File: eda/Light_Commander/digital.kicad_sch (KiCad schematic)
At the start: 36 parts, among them J14 USB_C_Receptacle_USB2.0_16P, Q1 MMBT3904, Q2 MMBT3904, Q3 MMBT3904, Q4 MMBT3904, SW2 SW_Push, U1 STM32F446RETx, U6 USBLC6-2SC6, Y1 8 MHz

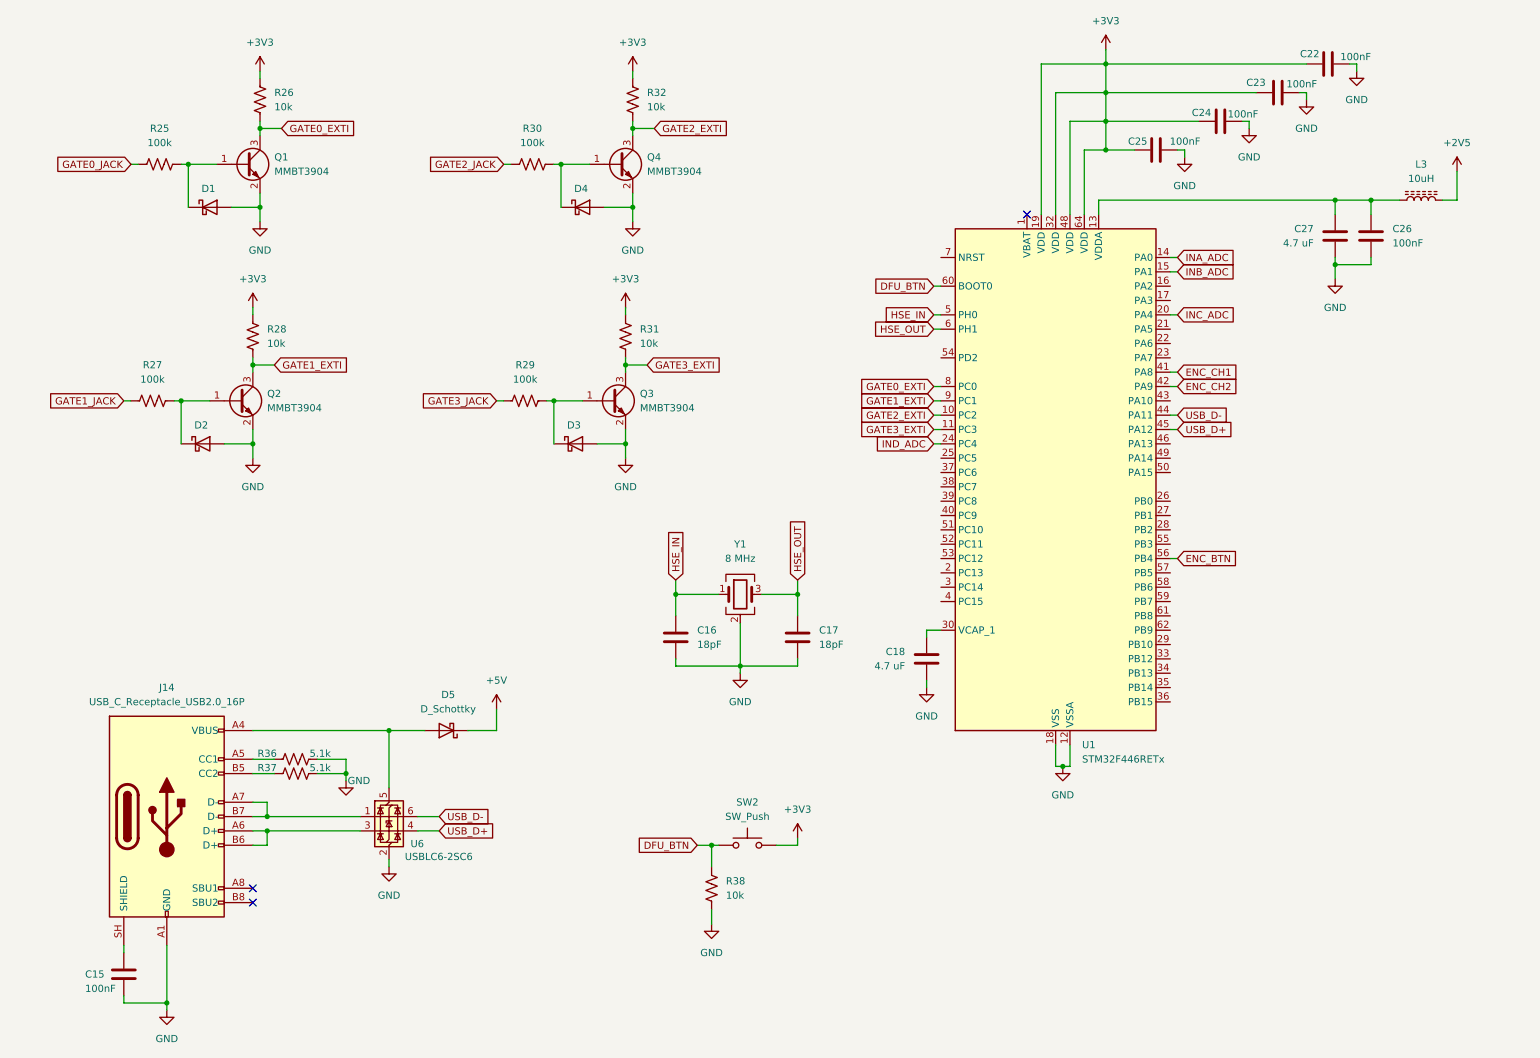
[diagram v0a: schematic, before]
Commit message: Add OLED, LED strip connector, and LED level shifter to schematic
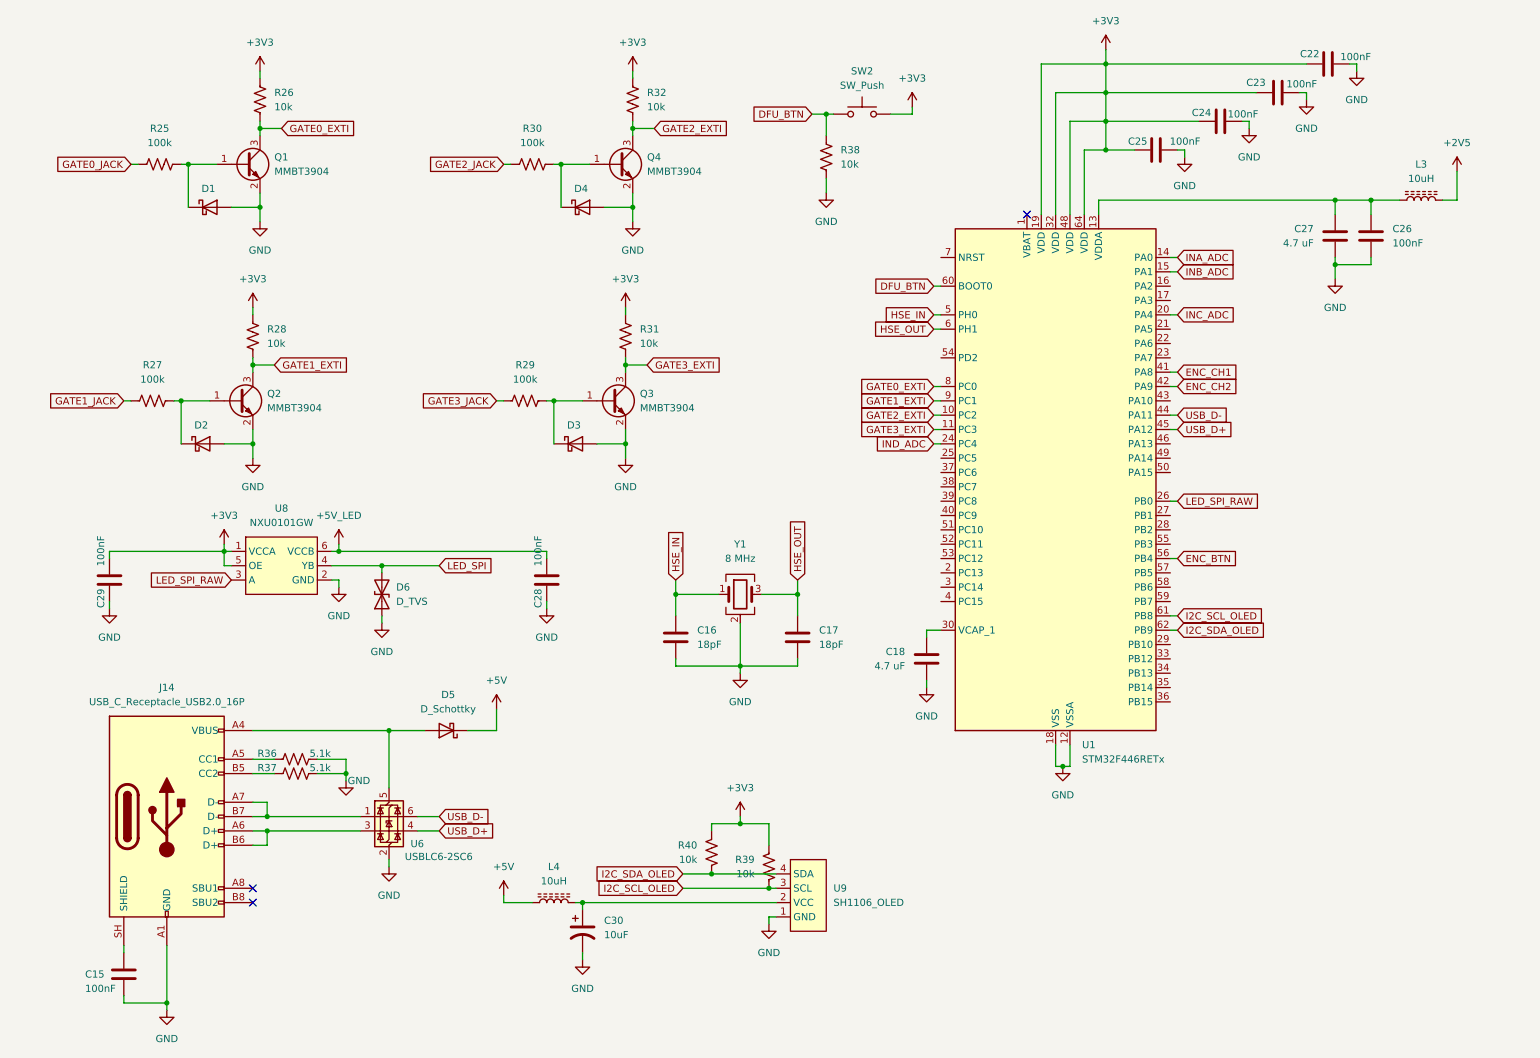
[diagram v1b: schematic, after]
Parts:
- added C28, C29: 100nF, Capacitor_SMD:C_0805_2012Metric, symbol Device:C
- added C30: 10uF, Capacitor_SMD:C_Elec_6.3x7.7, symbol Device:C_Polarized_US
- added D6: D_TVS, Diode_SMD:D_SOD-123F, symbol Device:D_TVS
- added L4: 10uH, Inductor_SMD:L_1210_3225Metric, symbol Device:L_Ferrite
- added R39, R40: 10k, Resistor_SMD:R_0805_2012Metric, symbol Device:R_US
- added U8: NXU0101GW, Package_TO_SOT_SMD:SOT-363_SC-70-6, symbol NXU0101GW:NXU0101GW
- added U9: SH1106_OLED, footprints:SH1106_1.3in_OLED, symbol SH1106_OLED:SH1106_OLED
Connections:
- net +3V3: now also C29.1, R39.1, R40.1, U8.1 (VCCA), U8.5 (OE)
- net +5V: now also L4.1
- net GND: now also C28.2, C29.2, C30.2, D6.1 (A1), U8.2 (GND), U9.1 (GND)
- net LED_SPI_RAW: now reaches U1.26 (PB0)
- net LED_SPI_RAW: now also U8.3 (A)
- net I2C_SCL_OLED: now reaches U1.61 (PB8)
- net I2C_SCL_OLED: now also R39.2, U9.3 (SCL)
- net I2C_SDA_OLED: now reaches U1.62 (PB9)
- net I2C_SDA_OLED: now also R40.2, U9.4 (SDA)
- new net: C30.1, L4.2, U9.2 (VCC)
- new net +5V_LED: C28.1, U8.6 (VCCB)
- new net LED_SPI: D6.2 (A2), U8.4 (YB)
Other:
- moved on the sheet: R38, SW2

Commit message: Add MDI in and thru to schematic
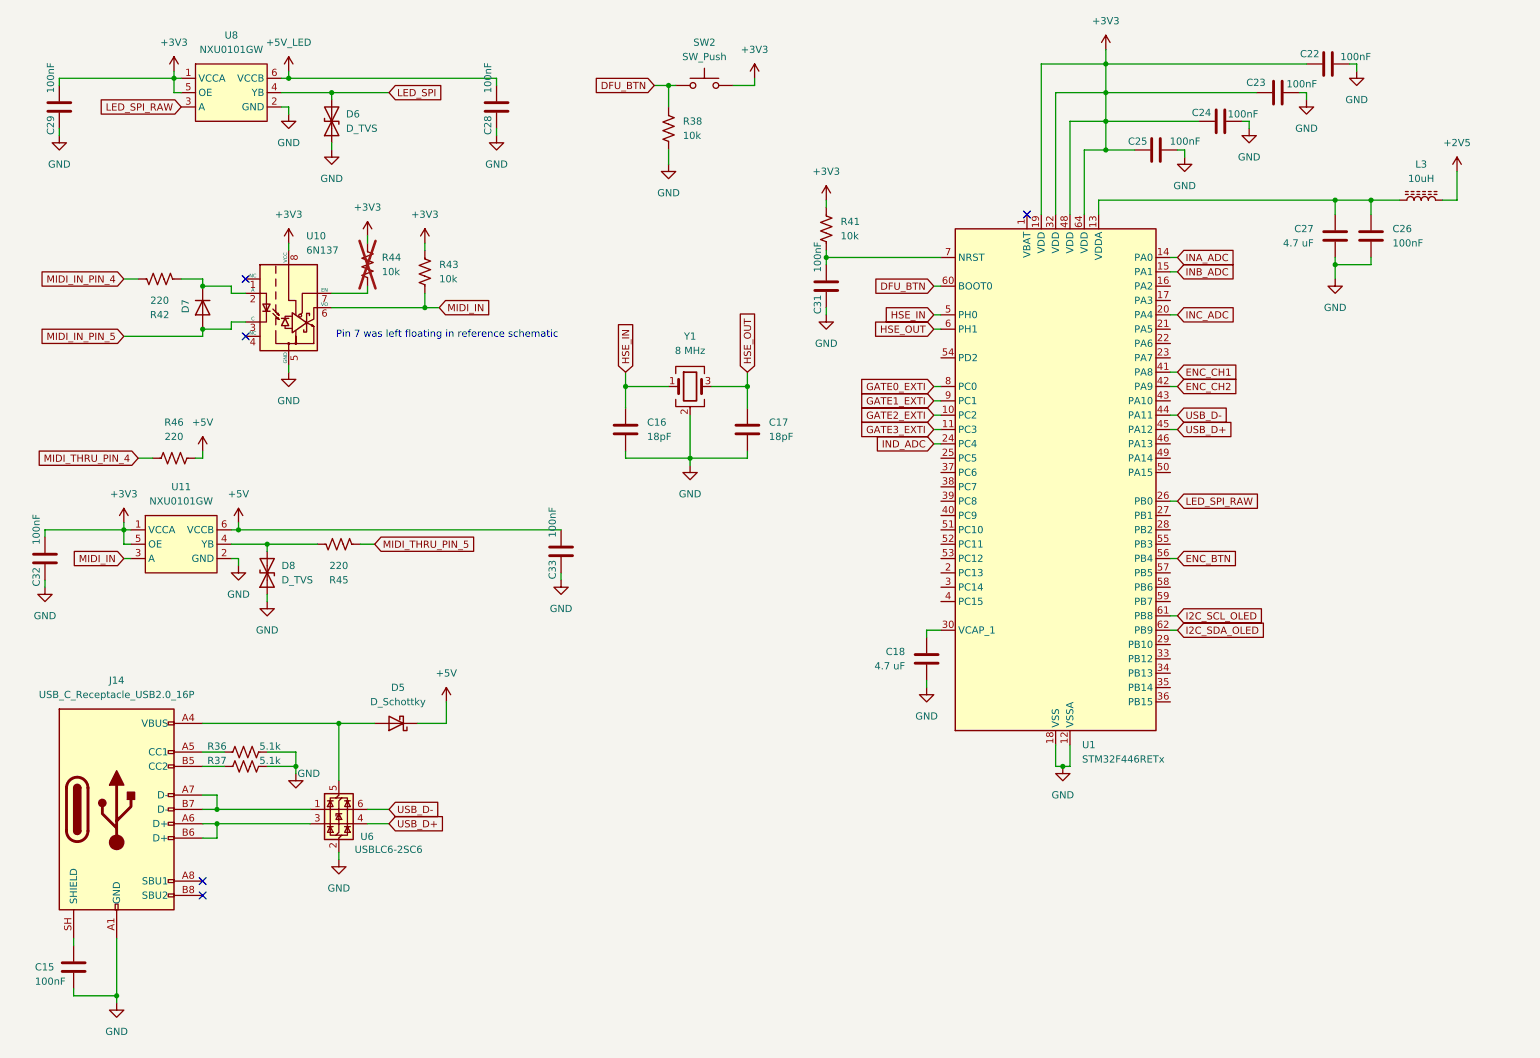
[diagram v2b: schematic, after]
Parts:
- removed C30: 10uF, Capacitor_SMD:C_Elec_6.3x7.7, symbol Device:C_Polarized_US
- removed D1, D2, D3, D4: GSBAT54W, Diode_SMD:D_SOD-123, symbol Device:D_Schottky
- removed L4: 10uH, Inductor_SMD:L_1210_3225Metric, symbol Device:L_Ferrite
- removed Q1, Q2, Q3, Q4: MMBT3904, Package_TO_SOT_SMD:SOT-23, symbol Transistor_BJT:MMBT3904
- removed R25, R27, R29, R30: 100k, Resistor_SMD:R_0805_2012Metric, symbol Device:R_US
- removed R26, R28, R31, R32, R39, R40: 10k, Resistor_SMD:R_0805_2012Metric, symbol Device:R_US
- removed U9: SH1106_OLED, footprints:SH1106_1.3in_OLED, symbol SH1106_OLED:SH1106_OLED
- added C31, C32, C33: 100nF, Capacitor_SMD:C_0805_2012Metric, symbol Device:C
- added D7: D, Diode_SMD:D_SOD-123, symbol Device:D
- added D8: D_TVS, Diode_SMD:D_SOD-123F, symbol Device:D_TVS
- added R41, R43, R44: 10k, Resistor_SMD:R_0805_2012Metric, symbol Device:R_US
- added R42, R45, R46: 220, Resistor_SMD:R_0805_2012Metric, symbol Device:R_US
- added U10: 6N137, Package_SO:SOP-8_6.605x9.655mm_P2.54mm, symbol Isolator:6N137
- added U11: NXU0101GW, Package_TO_SOT_SMD:SOT-363_SC-70-6, symbol NXU0101GW:NXU0101GW
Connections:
- net +3V3: now also C32.1, R41.1, R43.1, R44.1, U10.8 (VCC), U11.1 (VCCA), U11.5 (OE)
- net +5V: now also C33.1, R46.1, U11.6 (VCCB)
- net GND: now also C31.2, C32.2, C33.2, D8.1 (A1), U10.5 (GND), U11.2 (GND)
- net at U1.7 (NRST): now also C31.1, R41.2
- new net: R44.2, U10.7 (EN)
- new net: D8.2 (A2), R45.2, U11.4 (YB)
- new net: D7.1 (K), R42.1, U10.2 (A)
- new net MIDI_IN: R43.2, U10.6 (VO), U11.3 (A)
- new net MIDI_IN_PIN_4: R42.2
- new net MIDI_IN_PIN_5: D7.2 (A), U10.3 (C)
- new net MIDI_THRU_PIN_4: R46.2
- new net MIDI_THRU_PIN_5: R45.1
- no-connect marks 3 -> 5
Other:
- note added: "Pin 7 was left floating in reference schematic"
- moved on the sheet: C15, C16, C17, C28, C29, D5, D6, J14, R36, R37, R38, SW2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

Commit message: Add buttons, SWD, and LED reverse polarity protection to schematic
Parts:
- added D10, D9: D_TVS, Diode_SMD:D_SOD-123F, symbol Device:D_TVS
- added J18: Conn_01x03, Connector_PinHeader_2.54mm:PinHeader_1x03_P2.54mm_Vertical, symbol Connector_Generic:Conn_01x03
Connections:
- net GND: now also D10.1 (A1), D9.1 (A1), J18.3 (Pin_3)
- net MIDI_IN: now also U1.17 (PA3), D10.2 (A2), J18.2 (Pin_2)
- net MIDI_OUT: now reaches U1.16 (PA2)
- net MIDI_OUT: now also D9.2 (A2), J18.1 (Pin_1)
- net USART6_TX: now reaches U1.37 (PC6)
- net USART6_RX: now reaches U1.38 (PC7)
- net SWDIO: now reaches U1.46 (PA13)
- net SWCLK: now reaches U1.49 (PA14)
- net SWO: now reaches U1.55 (PB3)
- net NRST: now reaches C31.1, R41.2, U1.7 (NRST)
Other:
- note added: "DFU Trigger"
- note added: "LED SPI Level Shifter and ESD Protection"
- note added: "MCU"
- note added: "MCU Clock"
- note added: "MIDI Input"
- note added: "MIDI Thru + ESD Protection"
- note added: "ROUTE THESE LOL"
- note added: "Rear MIDI/UART connector"
- note added: "SIDE TEXT"
- note added: "USB C for DFU"
- moved on the sheet: C16, C17, Y1
